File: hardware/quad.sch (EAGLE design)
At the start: 18 parts, among them U101 STM32F427VGT6, X101 24MHz

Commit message: Add USB-UART, BNO055
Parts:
- removed J301, J302: (no value), quad:PINHD-1X50
- added C211, C401, C402, C403, C404: 100nF, quad:C-EUC0603
- added C212, C213, C405, C406: 10uF, quad:C-EUC0603
- added ESC1, ESC2, ESC3, ESC4: AFRO_ESC, quad:AFRO_ESC
- added IC1: BN055, quad:BNO055
- added MOT1, MOT2, MOT3, MOT4: MOTOR, quad:MOTOR
- added R101, R401: 10k, quad:R-US_R0603
- added R402, R403: 270, quad:R-US_R0603
- added RXLED, TXLED: LED, quad:LED
- added U201, U403: LD1117, quad:LD1117
- added U401: FT232R, quad:FT232R
- added U402: USB-MICROB", quad:USB-MICROB"
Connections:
- new net MOT1_1: ESC1.MOT1, MOT1.MOT1
- new net MOT1_2: ESC1.MOT2, MOT1.MOT2
- new net MOT1_3: ESC1.MOT3, MOT1.MOT3
- new net MOT2_1: ESC2.MOT1, MOT2.MOT1
- new net MOT_2_2: ESC2.MOT2, MOT2.MOT2
- new net MOT_2_3: ESC2.MOT3, MOT2.MOT3
- new net MOT_3_1: ESC3.MOT1, MOT3.MOT1
- new net MOT_3_2: ESC3.MOT2, MOT3.MOT2
- new net MOT_3_3: ESC3.MOT3, MOT3.MOT3
- new net MOT_4_1: ESC4.MOT1, MOT4.MOT1
- new net MOT_4_2: ESC4.MOT2, MOT4.MOT2
- new net MOT_4_3: ESC4.MOT3, MOT4.MOT3
- new net N$10: R402.2, RXLED.C
- new net N$11: R403.2, TXLED.C
- new net N$2: R401.1, U401.RESET#
- new net N$5: C401.1, U401.3V3OUT
- new net N$8: R403.1, U401.CBUS0
- new net N$9: R402.1, U401.CBUS1
- new net PWM1: ESC1.PWM
- new net PWM2: ESC2.PWM
- new net PWM3: ESC3.PWM
- new net PWM4: ESC4.PWM
- new net USBDM: U401.USBDM, U402.D-
- new net USBDP: U401.USBDP, U402.D+
- new net VBATT: C213.1, ESC1.VBAT, ESC2.VBAT, ESC3.VBAT, ESC4.VBAT, U201.VIN
- new net VBUS: C402.2, C403.1, C404.1, C405.1, R401.2, U401.VCC, U403.VIN
- net BOOT0: now also U401.DTR#; no longer J302.44
- net BOOT1: now also R101.1; no longer J301.37
- net CAN1_RX: no longer J302.31
- net CAN1_TX: no longer J302.32
- net CAN2_RX: no longer J302.41
- net CAN2_TX: no longer J302.42
- net GND: now also C211.2, C212.2, C213.2, C401.2, C402.1, C403.2, C404.2, C405.2, C406.2, ESC1.GND, ESC1.PWM_GND, ESC2.GND, ESC2.PWM_GND, ESC3.GND, ESC3.PWM_GND, ESC4.GND, ESC4.PWM_GND, R101.2, U201.GND, U401.GND, U401.TEST, U402.GND, U403.GND; no longer J301.10, J301.11, J301.12, J301.13, J301.19, J301.20, J301.21, J301.22, J301.27, J301.28, J301.49, J301.6, J302.23, J302.24, J302.25, J302.49, J302.50
- net I2C1_SCL: no longer J302.45
- net I2C1_SDA: no longer J302.46
- net I2C2_SCL: no longer J301.47
- net I2C2_SDA: no longer J301.48
- net I2C3_SCL: no longer J302.17
- net I2C3_SDA: no longer J302.16
- net JTCK-SWCLK: no longer J302.26
- net JTDI: no longer J302.27
- net JTDO/TRACESWO: no longer J302.39
- net JTMS-SWDIO: no longer J302.22
- net NJTRST: no longer J302.40
- net NRST: now also U401.RTS#; no longer J301.14
- net PA2: no longer J301.25
- net PA3: no longer J301.26
- net PA4: no longer J301.29
- net PB0: no longer J301.35
- net PB1: no longer J301.36
- net PB12: no longer J302.1
- net PB7: no longer J302.43
- net PC0: no longer J301.15
- net PC1: no longer J301.16
- net PC13: no longer J301.7
- net PC14: no longer J301.8
- net PC15: no longer J301.9
- net PC2: no longer J301.17
- net PC3: no longer J301.18
- net PC4: no longer J301.33
- net PC5: no longer J301.34
- net PC8: no longer J302.15
- net PD10: no longer J302.7
- net PD13: no longer J302.10
- net PD14: no longer J302.11
- net PD15: no longer J302.12
- net PD2: no longer J302.33
- net PD7: no longer J302.38
- net PE10: no longer J301.41
- net PE11: no longer J301.42
- net PE15: no longer J301.46
- net PE2: no longer J301.1
- net PE3: no longer J301.2
- net PE4: no longer J301.3
- net PE5: no longer J301.4
- net PE6: no longer J301.5
- net PE9: no longer J301.40
- net SPI1_MISO: no longer J301.31
- net SPI1_MOSI: no longer J301.32
- net SPI1_SCK: no longer J301.30
- net SPI2_MISO: no longer J302.3
- net SPI2_MOSI: no longer J302.4
- net SPI2_SCK: no longer J302.2
- net SPI3_MISO: no longer J302.29
- net SPI3_MOSI: no longer J302.30
- net SPI3_SCK: no longer J302.28
- net SPI4_MISO: no longer J301.44
- net SPI4_MOSI: no longer J301.45
- net SPI4_SCK: no longer J301.43
- net UART4_RX: no longer J301.24
- net UART4_TX: no longer J301.23
- net UART7_RX: no longer J301.38
- net UART7_TX: no longer J301.39
- net UART8_RX: no longer J302.47
- net UART8_TX: no longer J302.48
- net USART1_CTS: no longer J302.20
- net USART1_RTS: no longer J302.21
- net USART1_RX: now also U401.TXD; no longer J302.19
- net USART1_TX: now also U401.RXD; no longer J302.18
- net USART2_CTS: no longer J302.34
- net USART2_RTS: no longer J302.35
- net USART2_RX: no longer J302.37
- net USART2_TX: no longer J302.36
- net USART3_CTS: no longer J302.8
- net USART3_RTS: no longer J302.9
- net USART3_RX: no longer J302.6
- net USART3_TX: no longer J302.5
- net USART6_RX: no longer J302.14
- net USART6_TX: no longer J302.13
- net VDD_3V3: now also C211.1, C212.1, C406.1, RXLED.A, TXLED.A, U201.3V3, U401.VCCIO, U403.3V3; no longer J301.50
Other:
- note added: "BNO055"
- note added: "Extra Decoupling Capacitor No Placement Requirements"
- note added: "Motors and ESCs"
- note added: "Power Regulator"
- note added: "Pull high for bootloader"
- note added: "Regulator from USB Power"
- note added: "USB Power Decoupling Capacitors"
- note added: "USB to UART"
- note removed: "BREAKOUT PINS"

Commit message: Wire BNO055, Added XBEE
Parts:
- added BNO055_NBOOT_LOAD, BNO055_NRESET: TESTPAD, quad:TESTPAD
- added C501, C502: 0.1uF, quad:C-EUC0603
- added C503, C504: 22pF, quad:C-EUC0603
- added R1, R501, R502, R503: 10k, quad:R-US_R0603
- added U202, U203: SN74AHC1G32DBVR, quad:SN74AHC1G32DBVR
- added U701: AOD4189, quad:AOD4189
- added XB1: XBEE, quad:XBEE
- added Y501: 32.768kHz, quad:CRYSTAL
- C404: value 100nF -> 4.7uF
- IC1: value BN055 -> BNO055
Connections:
- new net FT232_DTR: U203.B, U401.DTR#
- new net FT232_RTS: U202.B, U401.RTS#
- new net N$12: IC1.17, R501.1
- new net N$13: BNO055_NRESET.PIN, IC1.11
- new net N$14: IC1.6, R503.1
- new net N$15: IC1.5, R502.1
- new net N$16: BNO055_NBOOT_LOAD.PIN, IC1.4, R1.1
- new net N$3: U701.D
- new net N$4: C501.2, IC1.9
- new net N$6: C504.2, IC1.27, Y501.2
- new net N$7: C503.2, IC1.26, Y501.1
- new net XBEE_DIO0: U202.A, XB1.AD0/DIO0
- new net XBEE_DIO1: U203.A, XB1.AD1/DIO1
- new net XBEE_DIO4: XB1.RF_TX/AD4/DIO4
- net BOOT0: now also U203.Y; no longer U401.DTR#
- net GND: now also C501.1, C502.1, C503.1, C504.1, IC1.10, IC1.15, IC1.16, IC1.18, IC1.2, IC1.25, R501.2, R502.2, R503.2, U202.GND, U203.GND, XB1.GND
- net I2C1_SCL: now also IC1.19
- net I2C1_SDA: now also IC1.20
- net NRST: now also U202.Y; no longer U401.RTS#
- net PB12: now also IC1.14
- net USART3_RX: now also XB1.DOUT
- net USART3_TX: now also XB1.DIN/!CONFIG
- net VBATT: now also U701.S
- net VDD_3V3: now also C502.2, IC1.28, IC1.3, R1.2, U202.VCC, U203.VCC, XB1.VCC
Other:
- note added: "BATTERY CONTROL"
- note added: "XBEE"

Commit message: Add power connectors, finish BNO055
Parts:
- removed U701: AOD4189, quad:AOD4189
- added J501: I2C_TEST, quad:PINHD-1X2
- added R2, R3: 10k, quad:R-US_R0603
- added U$1: XT60, quad:XT60
- U202: value SN74AHC1G32DBVR -> AND_GATE; device quad:SN74AHC1G32DBVR -> quad:AND_GATE
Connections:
- net SPI3_MOSI renamed PC12
- net USART3_CTS renamed PD11
- net USART3_RTS renamed PD12
- removed net SPI3_MISO: U101PORTC_H.PC11
- removed net SPI3_SCK: U101PORTC_H.PC10
- new net PD8: U101PORTD_H.PD8
- new net PD9: U101PORTD_H.PD9
- net GND: now also U$1.GND
- net I2C1_SCL: now also J501.2, R3.2
- net I2C1_SDA: now also J501.1, R2.2
- net N$3: now also U$1.PWR; no longer U701.D
- net USART3_RX: now also U101PORTC_H.PC11; no longer U101PORTD_H.PD9
- net USART3_TX: now also U101PORTC_H.PC10; no longer U101PORTD_H.PD8
- net VBATT: no longer U701.S
- net VDD_3V3: now also R2.1, R3.1
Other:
- note added: "Bootloader Selection Will be selected by either the XBEE or FT232R"

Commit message: First draft schematic done
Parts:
- added R701: 10k, quad:R-US_R0603
- added U$2: PSMN9RS-30YLC, quad:PSMN9RS-30YLC
- added U404: MFS201N-16-Z, quad:MFS201N-16-Z
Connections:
- removed net N$3: U$1.PWR
- new net KILL_GND: ESC1.GND, ESC2.GND, ESC3.GND, ESC4.GND, U$2.D
- new net POWER_EN: R701.2, U$2.G, U404.5
- net GND: now also R701.1, U$2.S; no longer ESC1.GND, ESC2.GND, ESC3.GND, ESC4.GND
- net VBATT: now also U$1.PWR, U404.3
- net VBUS: now also U404.1, U404.2
- net XBEE_DIO4: now also U404.6
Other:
- note added: "Kill Switch is only available on Battery Power On USB power, motor power is always killed"
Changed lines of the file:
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@@
 <part name="ESC2" library="quad" deviceset="AFRO_ESC" device=""/>
 <part name="GND14" library="quad" deviceset="GND" device=""/>
-<part name="GND16" library="quad" deviceset="GND" device=""/>
-<part name="GND17" library="quad" deviceset="GND" device=""/>
-<part name="GND18" library="quad" deviceset="GND" device=""/>
-<part name="GND19" library="quad" deviceset="GND" device=""/>
 <part name="GND20" library="quad" deviceset="GND" device=""/>
 <part name="GND21" library="quad" deviceset="GND" device=""/>
@@
 <part name="GND46" library="quad" deviceset="GND" device=""/>
 <part name="GND47" library="quad" deviceset="GND" device=""/>
+<part name="U404" library="quad" deviceset="MFS201N-16-Z" device=""/>
+<part name="U$2" library="quad" deviceset="PSMN9RS-30YLC" device=""/>
+<part name="R701" library="quad" deviceset="R-US_" device="R0603" value="10k"/>
+<part name="GND48" library="quad" deviceset="GND" device=""/>
 </parts>
 <sheets>
@@
 <instance part="ESC2" gate="G$1" x="177.8" y="165.1"/>
 <instance part="GND14" gate="1" x="60.96" y="109.22" rot="R180"/>
-<instance part="GND16" gate="1" x="43.18" y="81.28" rot="R270"/>
-<instance part="GND17" gate="1" x="43.18" y="157.48" rot="R270"/>
-<instance part="GND18" gate="1" x="157.48" y="157.48" rot="R270"/>
-<instance part="GND19" gate="1" x="157.48" y="81.28" rot="R270"/>
 <instance part="GND20" gate="1" x="175.26" y="109.22" rot="R180"/>
 <instance part="GND21" gate="1" x="175.26" y="185.42" rot="R180"/>
@@
 </segment>
 <segment>
-<pinref part="ESC3" gate="G$1" pin="GND"/>
-<pinref part="GND16" gate="1" pin="GND"/>
-</segment>
-<segment>
-<pinref part="ESC1" gate="G$1" pin="GND"/>
-<pinref part="GND17" gate="1" pin="GND"/>
-</segment>
-<segment>
-<pinref part="ESC2" gate="G$1" pin="GND"/>
-<pinref part="GND18" gate="1" pin="GND"/>
-</segment>
-<segment>
-<pinref part="ESC4" gate="G$1" pin="GND"/>
-<pinref part="GND19" gate="1" pin="GND"/>
-</segment>
-<segment>
 <pinref part="ESC4" gate="G$1" pin="PWM_GND"/>
 <pinref part="GND20" gate="1" pin="GND"/>
@@
 <wire x1="81.28" y1="157.48" x2="91.44" y2="157.48" width="0.1524" layer="91"/>
 <pinref part="MOT1" gate="G$1" pin="MOT3"/>
+</segment>
+</net>
+<net name="KILL_GND" class="0">
+<segment>
+<pinref part="ESC1" gate="G$1" pin="GND"/>
+<wire x1="45.72" y1="157.48" x2="38.1" y2="157.48" width="0.1524" layer="91"/>
+<label x="38.1" y="157.48" size="1.778" layer="95" rot="R180" xref="yes"/>
+</segment>
+<segment>
+<pinref part="ESC3" gate="G$1" pin="GND"/>
+<wire x1="45.72" y1="81.28" x2="38.1" y2="81.28" width="0.1524" layer="91"/>
+<label x="38.1" y="81.28" size="1.778" layer="95" rot="R180" xref="yes"/>
+</segment>
+<segment>
+<pinref part="ESC4" gate="G$1" pin="GND"/>
+<wire x1="160.02" y1="81.28" x2="149.86" y2="81.28" width="0.1524" layer="91"/>
+<label x="149.86" y="81.28" size="1.778" layer="95" rot="R180" xref="yes"/>
+</segment>
+<segment>
+<pinref part="ESC2" gate="G$1" pin="GND"/>
+<wire x1="160.02" y1="157.48" x2="149.86" y2="157.48" width="0.1524" layer="91"/>
+<label x="149.86" y="157.48" size="1.778" layer="95" rot="R180" xref="yes"/>
 </segment>
 </net>
@@
 <wire x1="53.34" y1="116.84" x2="25.4" y2="116.84" width="0.1524" layer="94"/>
 <text x="20.32" y="119.38" size="1.778" layer="94">USB Power Decoupling Capacitors</text>
-<wire x1="167.64" y1="106.68" x2="238.76" y2="106.68" width="0.1524" layer="94"/>
+<wire x1="170.18" y1="106.68" x2="238.76" y2="106.68" width="0.1524" layer="94"/>
 <wire x1="238.76" y1="106.68" x2="238.76" y2="76.2" width="0.1524" layer="94"/>
-<wire x1="238.76" y1="76.2" x2="167.64" y2="76.2" width="0.1524" layer="94"/>
-<wire x1="167.64" y1="76.2" x2="167.64" y2="106.68" width="0.1524" layer="94"/>
+<wire x1="238.76" y1="76.2" x2="170.18" y2="76.2" width="0.1524" layer="94"/>
+<wire x1="170.18" y1="76.2" x2="170.18" y2="106.68" width="0.1524" layer="94"/>
 <text x="167.64" y="109.22" size="1.27" layer="94">Regulator from USB Power</text>
+<text x="78.74" y="63.5" size="1.778" layer="94">Kill Switch is only available on Battery Power
+On USB power, motor power is always killed</text>
 </plain>
 <instances>
@@
 <instance part="C405" gate="G$1" x="177.8" y="93.98"/>
 <instance part="C406" gate="G$1" x="215.9" y="93.98"/>
+<instance part="U404" gate="G$1" x="119.38" y="88.9"/>
 </instances>
 <busses>
@@
 <pinref part="U403" gate="G$1" pin="VIN"/>
 <wire x1="177.8" y1="96.52" x2="185.42" y2="96.52" width="0.1524" layer="91"/>
-<wire x1="175.26" y1="96.52" x2="177.8" y2="96.52" width="0.1524" layer="91"/>
 <junction x="177.8" y="96.52"/>
-<label x="175.26" y="96.52" size="1.27" layer="95" rot="R180" xref="yes"/>
+<pinref part="U404" gate="G$1" pin="2"/>
+<wire x1="177.8" y1="96.52" x2="134.62" y2="96.52" width="0.1524" layer="91"/>
+</segment>
+<segment>
+<pinref part="U404" gate="G$1" pin="1"/>
+<wire x1="101.6" y1="101.6" x2="91.44" y2="101.6" width="0.1524" layer="91"/>
+<label x="91.44" y="101.6" size="1.778" layer="95" rot="R180" xref="yes"/>
 </segment>
 </net>
@@
 <wire x1="127" y1="157.48" x2="132.08" y2="157.48" width="0.1524" layer="91"/>
 <label x="132.08" y="157.48" size="1.27" layer="95" xref="yes"/>
+</segment>
+</net>
+<net name="VBATT" class="0">
+<segment>
+<pinref part="U404" gate="G$1" pin="3"/>
+<wire x1="101.6" y1="91.44" x2="91.44" y2="91.44" width="0.1524" layer="91"/>
+<label x="91.44" y="91.44" size="1.778" layer="95" rot="R180" xref="yes"/>
+</segment>
+</net>
+<net name="XBEE_DIO4" class="0">
+<segment>
+<pinref part="U404" gate="G$1" pin="6"/>
+<wire x1="101.6" y1="76.2" x2="91.44" y2="76.2" width="0.1524" layer="91"/>
+<label x="91.44" y="76.2" size="1.778" layer="95" rot="R180" xref="yes"/>
+</segment>
+</net>
+<net name="POWER_EN" class="0">
+<segment>
+<pinref part="U404" gate="G$1" pin="5"/>
+<wire x1="134.62" y1="81.28" x2="139.7" y2="81.28" width="0.1524" layer="91"/>
+<label x="139.7" y="81.28" size="1.778" layer="95" xref="yes"/>
 </segment>
 </net>
@@
 <instance part="U$1" gate="G$1" x="63.5" y="109.22"/>
 <instance part="GND46" gate="1" x="76.2" y="101.6"/>
-<instance part="GND47" gate="1" x="104.14" y="96.52"/>
+<instance part="GND47" gate="1" x="190.5" y="66.04"/>
+<instance part="U$2" gate="G$1" x="190.5" y="83.82"/>
+<instance part="R701" gate="G$1" x="172.72" y="78.74" rot="R90"/>
+<instance part="GND48" gate="1" x="172.72" y="71.12"/>
 </instances>
 <busses>
@@
 <net name="VBATT" class="0">
 <segment>
-<wire x1="114.554" y1="111.76" x2="129.54" y2="111.76" width="0.1524" layer="91"/>
-<label x="129.54" y="111.76" size="1.27" layer="95" xref="yes"/>
-</segment>
-</net>
-<net name="N$3" class="0">
-<segment>
 <pinref part="U$1" gate="G$1" pin="PWR"/>
 <wire x1="93.726" y1="111.76" x2="73.66" y2="111.76" width="0.1524" layer="91"/>
+<label x="93.98" y="111.76" size="1.778" layer="95" xref="yes"/>
 </segment>
 </net>
@@
 <segment>
 <pinref part="GND47" gate="1" pin="GND"/>
-<wire x1="104.14" y1="101.6" x2="104.14" y2="99.06" width="0.1524" layer="91"/>
-</segment>
-</net>
+<pinref part="U$2" gate="G$1" pin="S"/>
+<wire x1="190.5" y1="68.58" x2="190.5" y2="73.66" width="0.1524" layer="91"/>
+</segment>
+<segment>
+<pinref part="R701" gate="G$1" pin="1"/>
+<pinref part="GND48" gate="1" pin="GND"/>
+</segment>
+</net>
+<net name="POWER_EN" class="0">
+<segment>
+<pinref part="U$2" gate="G$1" pin="G"/>
+<wire x1="177.8" y1="83.82" x2="172.72" y2="83.82" width="0.1524" layer="91"/>
+<label x="167.64" y="83.82" size="1.778" layer="95" rot="R180" xref="yes"/>
+<pinref part="R701" gate="G$1" pin="2"/>
+<wire x1="172.72" y1="83.82" x2="167.64" y2="83.82" width="0.1524" layer="91"/>
+<junction x="172.72" y="83.82"/>
+</segment>
+</net>
+<net name="KILL_GND" class="0">
+<segment>
+<pinref part="U$2" gate="G$1" pin="D"/>
+<wire x1="190.5" y1="93.98" x2="190.5" y2="101.6" width="0.1524" layer="91"/>
+<label x="190.5" y="101.6" size="1.778" layer="95" rot="R90" xref="yes"/>
+</segment>
+</net>

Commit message: Fixes and start layout
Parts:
- removed C212, C213: 10uF, quad:C-EUC0603
- removed U201: LD1117, quad:LD1117
- added ASSOC, PWR: LED, quad:LED
- added R4: 270, quad:R-US_R0603
- added R5: (no value), quad:R-US_R0603
- C205, C206, C207, C208, C209, C210, C401, C402, C403: value 100nF -> 0.1uF
- C211: value 100nF -> 4.7uF
- U402: value USB-MICROB" -> USB-MICROB; device quad:USB-MICROB" -> quad:USB-MICROB
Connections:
- new net N$17: R4.2, XB1.ASSOC/AD5/DIO5
- new net N$18: PWR.C, R5.2
- new net N$3: ASSOC.A, R4.1
- net GND: now also ASSOC.C, R5.1, U402.SHIELD; no longer C212.2, C213.2, U201.GND
- net VBATT: no longer C213.1, U201.VIN
- net VDD_3V3: now also PWR.A; no longer C212.1, U201.3V3
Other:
- note added: "Power LED"
- note removed: "Power Regulator"

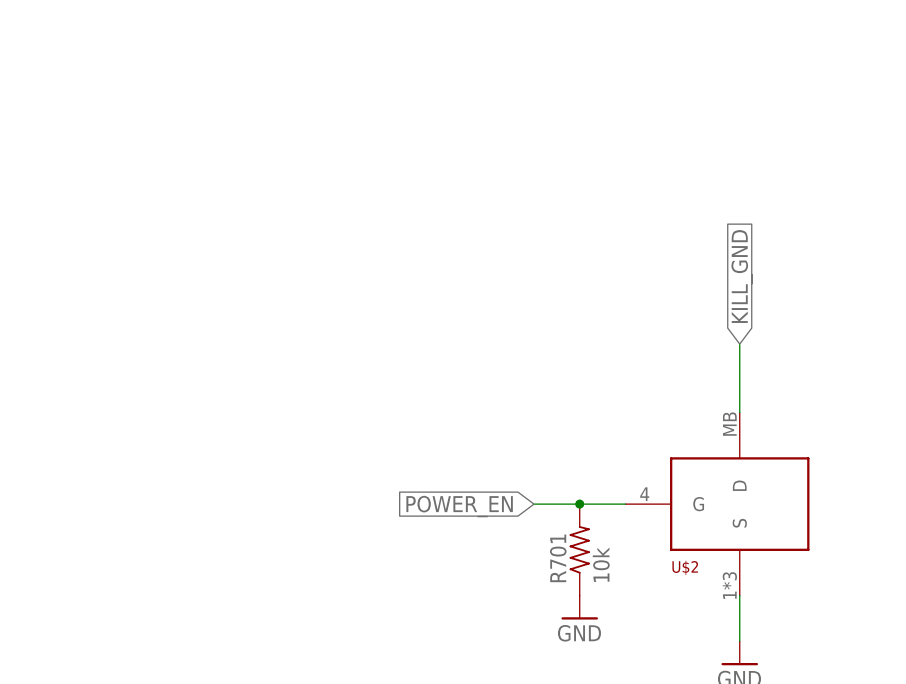
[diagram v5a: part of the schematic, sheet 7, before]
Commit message: Add board outline and make some placements
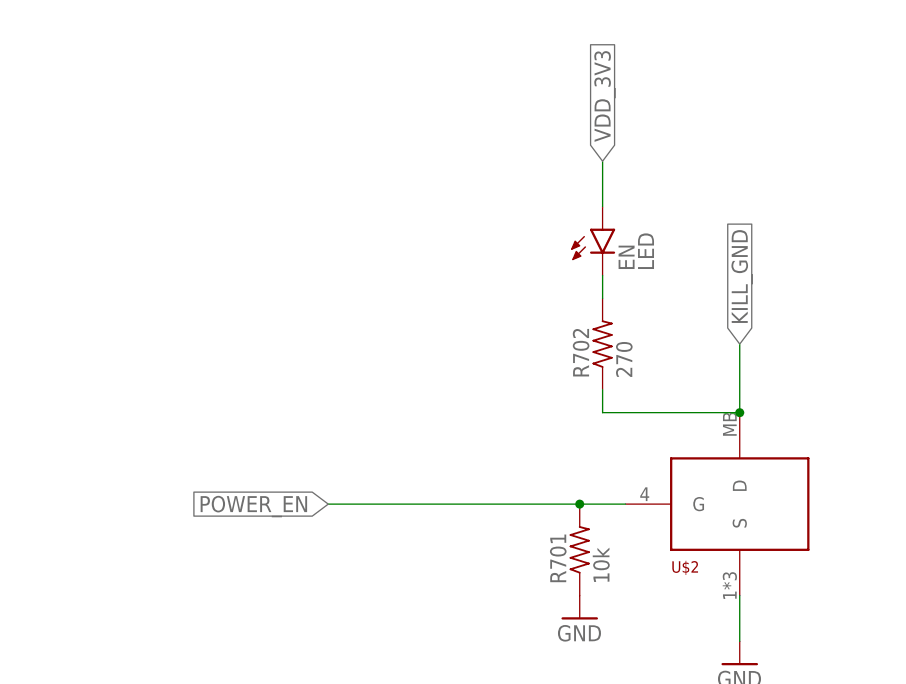
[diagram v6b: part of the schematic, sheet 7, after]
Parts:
- added EN: LED, quad:LED
- added R702: 270, quad:R-US_R0603
- R5: value (none) -> 270
- renumbered BNO055_NBOOT_LOAD to BNO_NBOOTLD, BNO055_NRESET to BNO_NRST, R1 to R504, R2 to R505, R3 to R506, R4 to R601
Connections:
- net USBDM renamed USB_D_N
- net USBDP renamed USB_D_P
- new net N$19: EN.C, R702.2
- new net PWR: C405.1, U403.VIN, U404.2
- net KILL_GND: now also R702.1
- net PB12: no longer IC1.14
- net PD2: now also IC1.14
- net VBUS: now also U402.VBUS; no longer C405.1, U403.VIN, U404.2
- net VDD_3V3: now also EN.A
